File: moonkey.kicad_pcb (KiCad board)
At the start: 2 copper layers, 34 parts

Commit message: update
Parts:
- removed REF** (x32): SW_Cherry_MX_PCB_1.00u, Switch_Keyboard_Cherry_MX:SW_Cherry_MX_PCB_1.00u
- removed REF** (x2): SW_Cherry_MX_PCB_1.50u_90deg, Switch_Keyboard_Cherry_MX:SW_Cherry_MX_PCB_1.50u_90deg
- added D1: 1N4148, Diode_THT:D_DO-35_SOD27_P7.62mm_Horizontal, F.Cu at (128.8, 118.4)
- added D10: 1N4148, Diode_THT:D_DO-35_SOD27_P7.62mm_Horizontal, F.Cu at (146.1, 114.8)
- added D11: 1N4148, Diode_THT:D_DO-35_SOD27_P7.62mm_Horizontal, F.Cu at (146.1, 117.3)
- added D12: 1N4148, Diode_THT:D_DO-35_SOD27_P7.62mm_Horizontal, F.Cu at (146.1, 119.9)
- added D13: 1N4148, Diode_THT:D_DO-35_SOD27_P7.62mm_Horizontal, F.Cu at (146.1, 130.0)
- added D14: 1N4148, Diode_THT:D_DO-35_SOD27_P7.62mm_Horizontal, F.Cu at (146.1, 122.4)
- added D15: 1N4148, Diode_THT:D_DO-35_SOD27_P7.62mm_Horizontal, F.Cu at (146.1, 125.0)
- added D16: 1N4148, Diode_THT:D_DO-35_SOD27_P7.62mm_Horizontal, F.Cu at (146.1, 127.5)
- added D17: 1N4148, Diode_THT:D_DO-35_SOD27_P7.62mm_Horizontal, F.Cu at (146.1, 132.6)
- added D2: 1N4148, Diode_THT:D_DO-35_SOD27_P7.62mm_Horizontal, F.Cu at (128.8, 115.8)
- added D3: 1N4148, Diode_THT:D_DO-35_SOD27_P7.62mm_Horizontal, F.Cu at (128.8, 113.3)
- added D4: 1N4148, Diode_THT:D_DO-35_SOD27_P7.62mm_Horizontal, F.Cu at (128.8, 126.0)
- added D5: 1N4148, Diode_THT:D_DO-35_SOD27_P7.62mm_Horizontal, F.Cu at (128.8, 123.4)
- added D6: 1N4148, Diode_THT:D_DO-35_SOD27_P7.62mm_Horizontal, F.Cu at (128.8, 120.9)
- added D7: 1N4148, Diode_THT:D_DO-35_SOD27_P7.62mm_Horizontal, F.Cu at (128.8, 133.6)
- added D8: 1N4148, Diode_THT:D_DO-35_SOD27_P7.62mm_Horizontal, F.Cu at (128.8, 131.1)
- added D9: 1N4148, Diode_THT:D_DO-35_SOD27_P7.62mm_Horizontal, F.Cu at (128.8, 128.5)
- added J1: AudioJack4, moonkey:PJ320A, F.Cu at (194.8, 115.8)
- added RZ1: RP2040-Zero, moonkey:RP2040, F.Cu at (124.9, 134.9)
- added SW1: SW_Push, moonkey:Cherry_1u_rev, F.Cu at (113.5, 61.0)
- added SW10: SW_Push, moonkey:Cherry_1u_rev, F.Cu at (170.7, 56.3)
- added SW11: SW_Push, moonkey:Cherry_1u_rev, F.Cu at (170.7, 75.3)
- added SW12: SW_Push, moonkey:Cherry_1u_rev, F.Cu at (170.7, 94.4)
- added SW13: SW_Push, moonkey:Cherry_1u_rev, F.Cu at (170.8, 122.6)
- added SW14: SW_Push, moonkey:Cherry_1u_rev, F.Cu at (189.7, 58.3)
- added SW15: SW_Push, moonkey:Cherry_1u_rev, F.Cu at (189.7, 77.4)
- added SW16: SW_Push, moonkey:Cherry_1u_rev, F.Cu at (189.7, 96.4)
- added SW17: SW_Push, moonkey:Cherry_1u_rev, F.Cu at (189.9, 125.0)
- added SW2: SW_Push, moonkey:Cherry_1u_rev, F.Cu at (113.5, 80.1)
- added SW3: SW_Push, moonkey:Cherry_1u_rev, F.Cu at (113.5, 99.1)
- added SW4: SW_Push, moonkey:Cherry_1u_rev, F.Cu at (132.6, 58.6)
- added SW5: SW_Push, moonkey:Cherry_1u_rev, F.Cu at (132.6, 77.7)
- added SW6: SW_Push, moonkey:Cherry_1u_rev, F.Cu at (132.6, 96.7)
- added SW7: SW_Push, moonkey:Cherry_1u_rev, F.Cu at (151.6, 58.6)
- added SW8: SW_Push, moonkey:Cherry_1u_rev, F.Cu at (151.6, 77.7)
- added SW9: SW_Push, moonkey:Cherry_1u_rev, F.Cu at (151.6, 96.7)
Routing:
- net ROW4: track 0.00 -> 180.7 mm, vias 0 -> 1
- net ROW3: track 0.00 -> 153.7 mm, vias 0 -> 2
- net +5V: track 0.00 -> 108.0 mm, vias 0 -> 2
- net Net-(D7-Pad2): track 0.00 -> 102.8 mm
- net ROW2: track 0.00 -> 99.8 mm
- net Net-(D14-Pad2): track 0.00 -> 93.5 mm
- net Earth: track 0.00 -> 93.1 mm, vias 0 -> 1
- net ROW1: track 0.00 -> 92.6 mm
- net SPI0_TX: track 0.00 -> 90.8 mm, vias 0 -> 2
- net Net-(D1-Pad2): track 0.00 -> 83.4 mm
- net SPI0_RX: track 0.00 -> 81.5 mm, vias 0 -> 2
- net Net-(D8-Pad2): track 0.00 -> 80.6 mm
- net ROW0: track 0.00 -> 79.5 mm
- net Net-(D4-Pad2): track 0.00 -> 79.0 mm
- net COL2: track 0.00 -> 78.0 mm, vias 0 -> 4
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
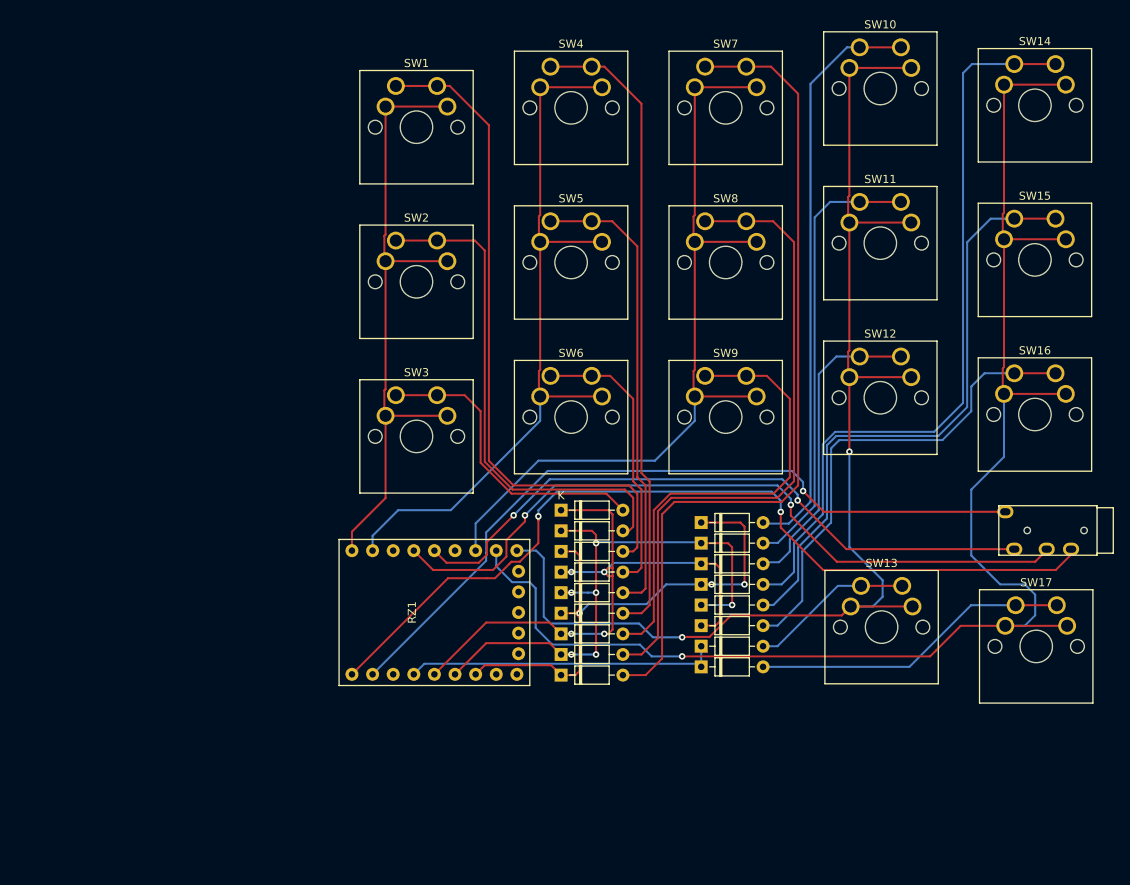
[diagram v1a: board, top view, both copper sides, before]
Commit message: keyboard layout chagned, scheme update(pins change)
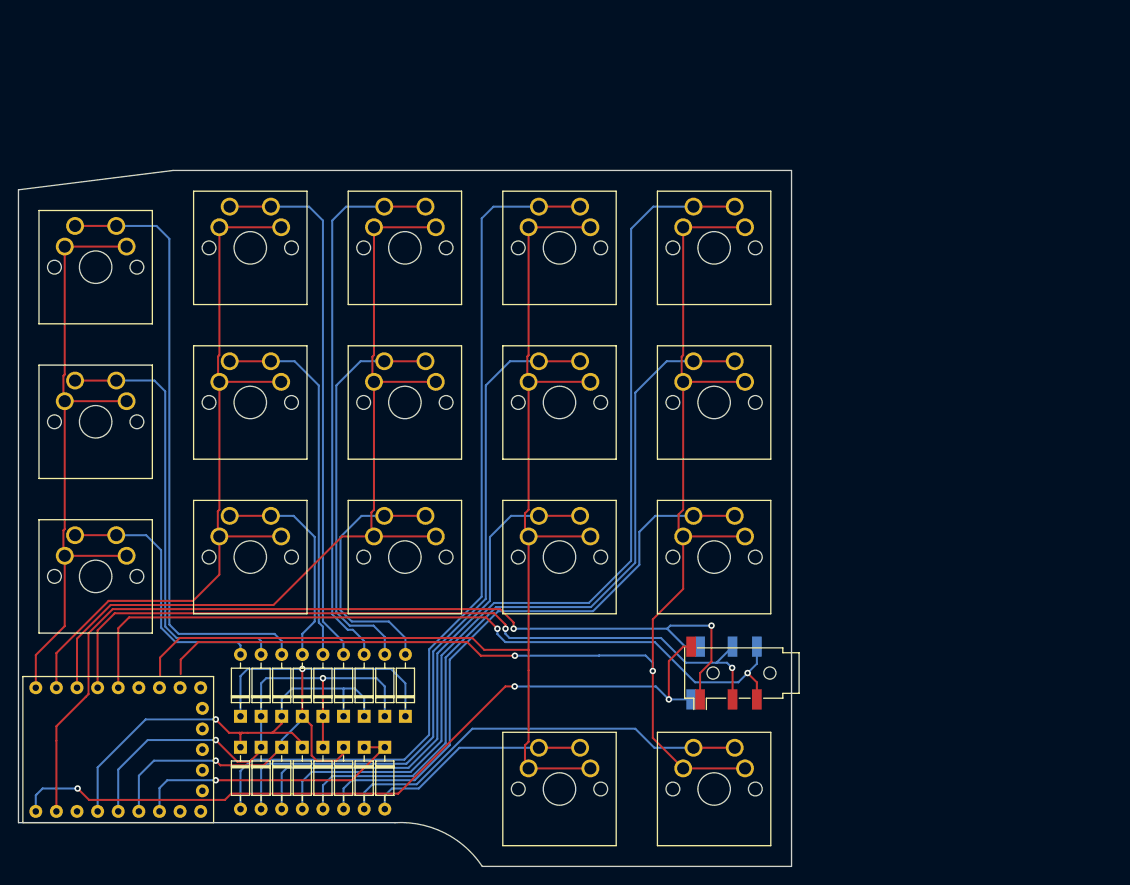
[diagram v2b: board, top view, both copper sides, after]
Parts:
- J1: footprint moonkey:PJ320A -> moonkey:PJ320D_rev; moved to B.Cu
- moved D10 63.2 mm to (89.3, 142.5), turned to -90 degrees
- moved D11 59.8 mm to (91.8, 142.5), turned to -90 degrees
- moved D12 56.4 mm to (94.4, 142.5), turned to -90 degrees
- moved D14 53.1 mm to (96.9, 142.5), turned to -90 degrees
- moved D15 49.8 mm to (99.4, 142.5), turned to -90 degrees
- moved J1 48.4 mm to (149.7, 133.3), turned to 180 degrees
- moved D3 47.0 mm to (89.3, 138.7), turned to 90 degrees
- moved D16 46.5 mm to (102.0, 142.5), turned to -90 degrees
- moved SW13 44.4 mm to (131.1, 142.6)
- moved SW11 44.1 mm to (131.1, 94.9)
- moved SW12 44.1 mm to (131.1, 114.0)
- moved SW10 44.1 mm to (131.1, 75.9)
- moved D2 43.5 mm to (91.8, 138.7), turned to 90 degrees
- moved SW17 43.4 mm to (150.2, 142.6)
- moved SW14 43.3 mm to (150.2, 75.9)
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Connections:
- RZ1 pad 17: COL0 -> COL3
- RZ1 pad 18: COL1 -> COL2
- RZ1 pad 19: COL2 -> COL1
- RZ1 pad 20: COL3 -> COL0
- RZ1 pad 3: unconnected-(RZ1-Pad3) -> ROW2
- RZ1 pad 7: ROW2 -> unconnected-(RZ1-Pad7)
- RZ1 pad 8: ROW4 -> unconnected-(RZ1-Pad8)
- RZ1 pad 9: ROW3 -> unconnected-(RZ1-Pad9)
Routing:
- net Net-(D10-Pad2): track 71.5 -> 108.8 mm
- net Net-(D7-Pad2): track 102.8 -> 67.7 mm
- net Net-(D11-Pad2): track 55.2 -> 86.6 mm
- net Net-(D8-Pad2): track 80.6 -> 49.6 mm
- net Net-(D12-Pad2): track 38.2 -> 65.1 mm
- net Net-(D9-Pad2): track 57.9 -> 32.0 mm
- net Earth: track 93.1 -> 117.8 mm, vias 1 -> 2
- net Net-(D14-Pad2): track 93.5 -> 116.2 mm
- net Net-(D15-Pad2): track 75.3 -> 93.8 mm
- net ROW4: track 180.7 -> 163.8 mm, vias 1 -> 2
- net SPI0_RX: track 81.5 -> 97.1 mm
- net Net-(D16-Pad2): track 59.6 -> 73.2 mm
- net Net-(D17-Pad2): track 39.3 -> 51.9 mm
- net Net-(D4-Pad2): track 79.0 -> 66.7 mm
- net Net-(D5-Pad2): track 57.6 -> 45.6 mm
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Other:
- board outline added: 95.2 x 85.8 mm

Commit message: uptate: ortholinear
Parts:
- moved SW1 2.38 mm to (74.0, 75.9)
- moved SW2 2.38 mm to (74.0, 94.9)
- moved SW3 2.38 mm to (74.0, 114.0)
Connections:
- RZ1 pad 7: unconnected-(RZ1-Pad7) -> ROW3
- RZ1 pad 8: unconnected-(RZ1-Pad8) -> ROW4
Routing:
- net ROW0: track 79.0 -> 81.9 mm
- net COL3: track 35.3 -> 37.8 mm
- net ROW4: track 163.8 -> 165.5 mm
- net ROW3: track 147.2 -> 148.8 mm
- net Net-(D3-Pad2): track 32.7 -> 33.9 mm
- net Net-(D2-Pad2): track 54.9 -> 55.4 mm
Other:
- board size 95.2 x 85.8 mm -> 95.7 x 86.2 mm
